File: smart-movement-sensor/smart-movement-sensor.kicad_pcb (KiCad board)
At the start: 2 copper layers, 22 parts, among them J1 ESP8266, Q1 2n2222, Q2 2n2222, Q3 2n2222, Q4 2n2222, U1 USB micro B, U2 movement sensor, U3 SN74AHC1G86DBVR, U4 LD1117V33C, U5 battery

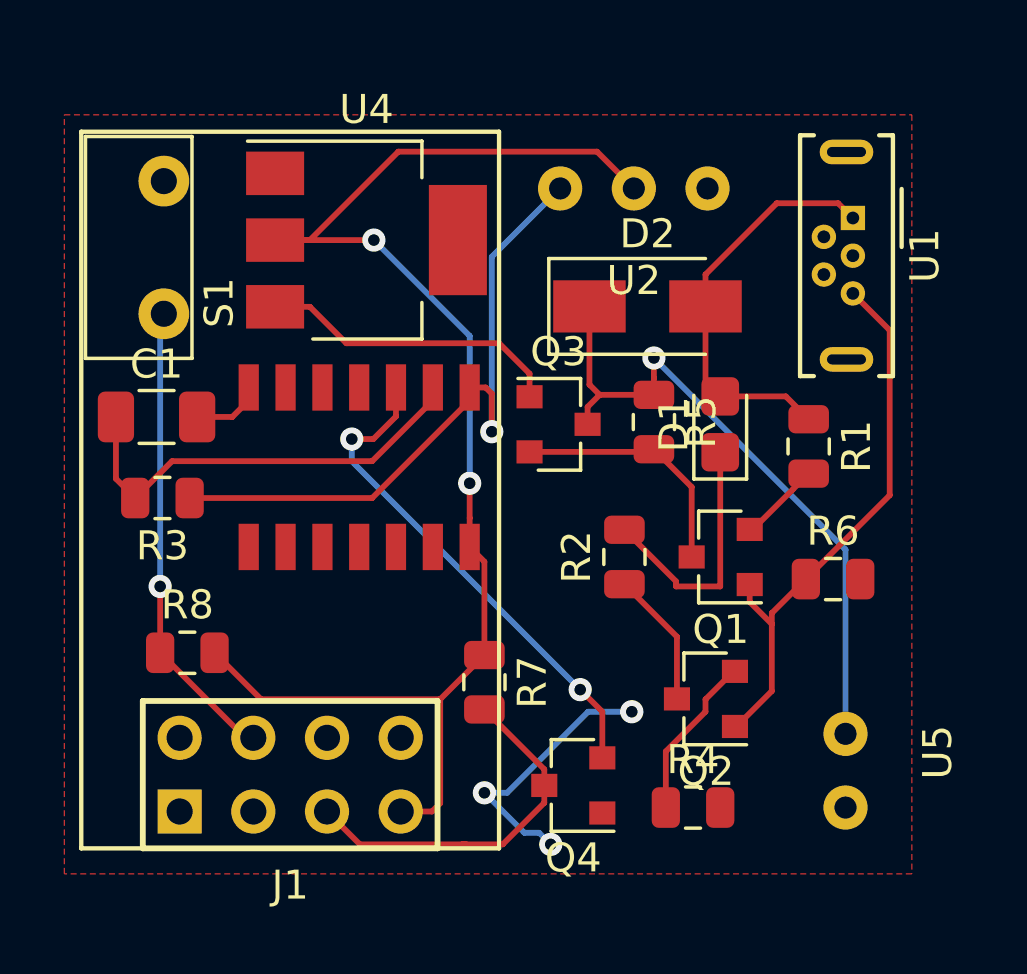
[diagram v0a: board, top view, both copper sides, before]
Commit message: Update smart switch 3d model
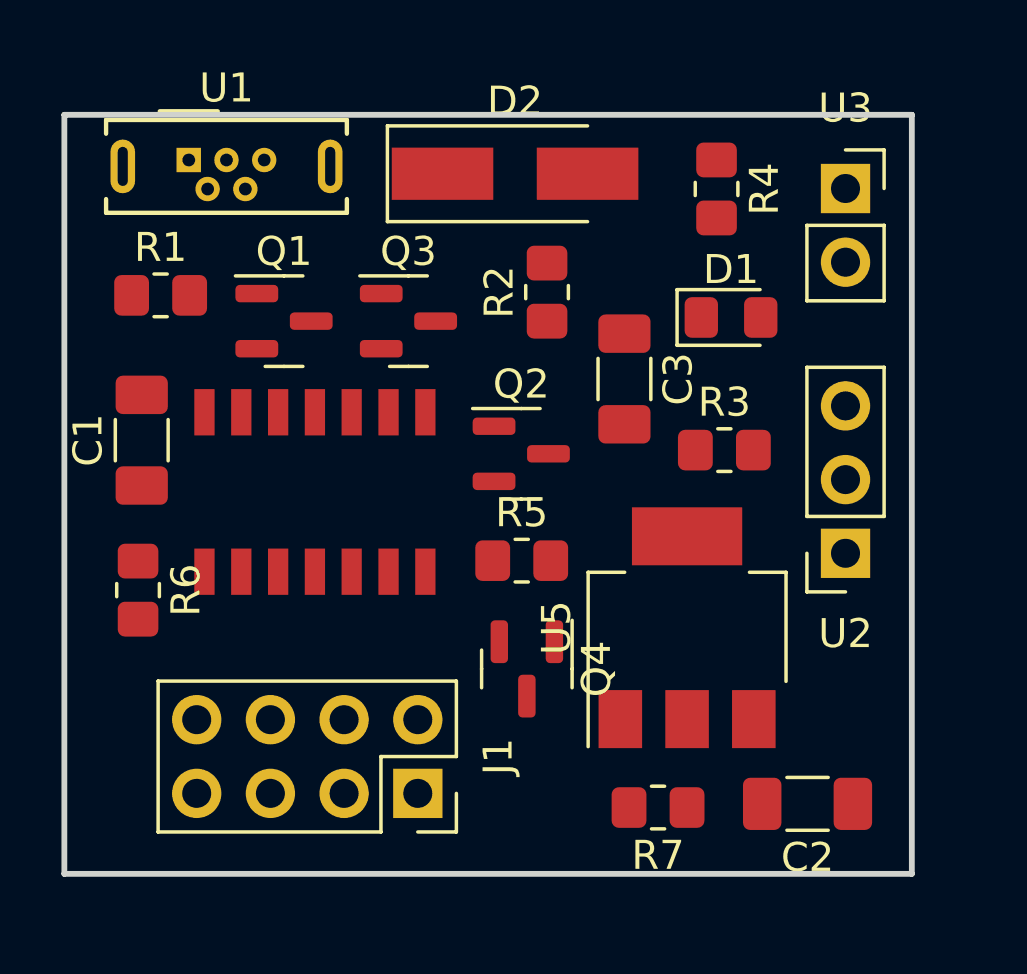
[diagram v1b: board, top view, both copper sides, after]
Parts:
- removed R8: 1k, fooprint:R_0805_2012Metric
- removed S1: switch, fooprint:SW_Tactile
- added C2: 100nF, Capacitor_SMD:C_1206_3216Metric_Pad1.33x1.80mm_HandSolder, F.Cu at (152.9, 101.0)
- added C3: 10uF, Capacitor_SMD:C_1206_3216Metric_Pad1.33x1.80mm_HandSolder, F.Cu at (146.6, 86.3)
- C1: value 1uF -> 2.2uF; footprint fooprint:C_1206_3216Metric -> Capacitor_SMD:C_1206_3216Metric_Pad1.33x1.80mm_HandSolder
- D1: footprint fooprint:LED_0805 -> LED_SMD:LED_0805_2012Metric_Pad1.15x1.40mm_HandSolder
- D2: footprint fooprint:D_SMA -> Diode_SMD:D_SMA_Handsoldering
- J1: footprint fooprint:ESP8266 -> Connector_PinSocket_2.54mm:PinSocket_2x04_P2.54mm_Vertical
- Q1, Q2, Q3, Q4: footprint fooprint:SOT-23 -> Package_TO_SOT_SMD:SOT-23
- R1, R2, R7: footprint fooprint:R_0805_2012Metric -> Resistor_SMD:R_0805_2012Metric_Pad1.20x1.40mm_HandSolder
- R3: value 1k -> 1R; footprint fooprint:R_0805_2012Metric -> Resistor_SMD:R_0805_2012Metric_Pad1.20x1.40mm_HandSolder
- R4: value 1R -> 1k; footprint fooprint:R_0805_2012Metric -> Resistor_SMD:R_0805_2012Metric_Pad1.20x1.40mm_HandSolder
- R5: value 1k -> 7.5R; footprint fooprint:R_0805_2012Metric -> Resistor_SMD:R_0805_2012Metric_Pad1.20x1.40mm_HandSolder
- R6: value 7.5R -> 1k; footprint fooprint:R_0805_2012Metric -> Resistor_SMD:R_0805_2012Metric_Pad1.20x1.40mm_HandSolder
- U2: footprint fooprint:MS_3pins -> Connector_PinSocket_2.54mm:PinSocket_1x03_P2.54mm_Vertical
- U3: value SN74AHC1G86DBVR -> battery; footprint fooprint:SOP14 -> Connector_PinSocket_2.54mm:PinSocket_1x02_P2.54mm_Vertical
- U4: value LD1117V33C -> SN74AHC1G86DBVR; footprint fooprint:SOT-223 -> footprints:SOP14
- U5: value battery -> LD1117V33C; footprint fooprint:battery_603040 -> Package_TO_SOT_SMD:SOT-223
- moved R6 24.0 mm to (129.8, 93.6), turned to -90 degrees
- moved U1 23.0 mm to (131.5, 78.8), turned to 0 degrees
- moved R1 22.9 mm to (130.6, 83.4), turned to 0 degrees
- moved R4 21.3 mm to (149.7, 79.8), turned to -90 degrees
- moved R3 19.4 mm to (150.0, 88.8), turned to 0 degrees
- moved U3 19.3 mm to (154.2, 79.8), turned to 0 degrees
- moved Q1 17.1 mm to (134.8, 84.3), turned to 0 degrees
- moved U2 14.5 mm to (154.2, 92.3), turned to 180 degrees
- moved Q2 10.6 mm to (143.0, 88.9), turned to 0 degrees
- moved R2 9.51 mm to (143.9, 83.3)
- moved U4 8.86 mm to (135.9, 90.2)
- moved R7 7.38 mm to (147.7, 101.1), turned to 180 degrees
- moved U5 7.36 mm to (148.7, 94.9)
- moved R5 6.60 mm to (143.0, 92.6), turned to 0 degrees
- moved D2 6.46 mm to (142.8, 79.2)
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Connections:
- net Net-(J1-Pad3) renamed /reset signal (no)
- C1 pad 1: Net-(C1-Pad1) -> /sensor signal delayed
- J1 pad 1: Net-(J1-Pad1) -> unconnected-(J1-Pad1)
- J1 pad 2: Net-(J1-Pad2) -> unconnected-(J1-Pad2)
- J1 pad 4: +3V3 -> +3.3V
- J1 pad 5: Net-(J1-Pad5) -> unconnected-(J1-Pad5)
- J1 pad 6: Net-(J1-Pad6) -> unconnected-(J1-Pad6)
- J1 pad 7: Net-(J1-Pad7) -> unconnected-(J1-Pad7)
- J1 pad 8: GND -> unconnected-(J1-Pad8)
- Q3 pad 2: Net-(Q3-Pad2) -> battery voltage
- Q4 pad 1: Net-(Q4-Pad1) -> /reset signal
- R3 pad 1: Net-(R3-Pad1) -> Net-(Q2-Pad1)
- R3 pad 2: Net-(C1-Pad1) -> GND
- R4 pad 1: Net-(Q2-Pad1) -> Net-(D2-Pad1)
- R4 pad 2: GND -> Net-(Q1-Pad3)
- R5 pad 1: Net-(D2-Pad1) -> Earth
- R5 pad 2: Net-(Q1-Pad3) -> GND
- R6 pad 1: Earth -> /sensor signal
- R6 pad 2: GND -> /sensor signal delayed
- R7 pad 1: +3V3 -> +3.3V
- U1 pad 2: Net-(U1-Pad2) -> unconnected-(U1-Pad2)
- U1 pad 3: Net-(U1-Pad3) -> unconnected-(U1-Pad3)
- U1 pad 4: Net-(U1-Pad4) -> unconnected-(U1-Pad4)
- U1 pad 6: Net-(U1-Pad6) -> Earth
- U2 pad 2: +3V3 -> +3.3V
- U2 pad 3: Net-(R3-Pad1) -> /sensor signal
- U3 pad 1: Net-(R3-Pad1) -> Net-(D2-Pad1)
- U3 pad 2: Net-(C1-Pad1) -> GND
- U4 pad 1: GND -> /sensor signal
- U4 pad 2: +3V3 -> /sensor signal delayed
- U4 pad 3: Net-(Q3-Pad2) -> /reset signal
- U5 pad 1: Net-(D2-Pad1) -> GND
- U5 pad 2: GND -> +3.3V
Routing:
- net +3V3: track 49.1 -> 0.00 mm, vias 2 -> 0
- net Net-(D2-Pad1): track 23.2 -> 0.00 mm, vias 1 -> 0
- net Net-(R3-Pad1): track 23.0 -> 0.00 mm, vias 1 -> 0
- net Earth: track 19.4 -> 0.00 mm
- net Net-(Q4-Pad1): track 17.4 -> 0.00 mm, vias 2 -> 0
- net Net-(J1-Pad7): track 16.2 -> 0.00 mm, vias 1 -> 0
- net Net-(C1-Pad1): track 15.2 -> 0.00 mm
- net Net-(D1-Pad2): track 14.1 -> 0.00 mm
- net /reset signal (no): track 12.8 -> 0.00 mm
- net GND: track 11.7 -> 0.00 mm, vias 3 -> 0
- net Net-(Q3-Pad2): track 10.5 -> 0.00 mm
- net Net-(D1-Pad1): track 8.84 -> 0.00 mm
- net Net-(Q1-Pad3): track 8.58 -> 0.00 mm
- net Net-(Q2-Pad1): track 5.71 -> 0.00 mm
- net Net-(Q2-Pad3): track 4.70 -> 0.00 mm
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- added copper zone on B.Cu, net GND
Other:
- board outline added: 29.2 x 26.2 mm
- net class Default removed
